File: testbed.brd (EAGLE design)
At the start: 50 x 31 mm, 22 parts, among them IC1 OPAMP-DUALMS, IC2 V_REG_MIC2920, Q1 BTS117

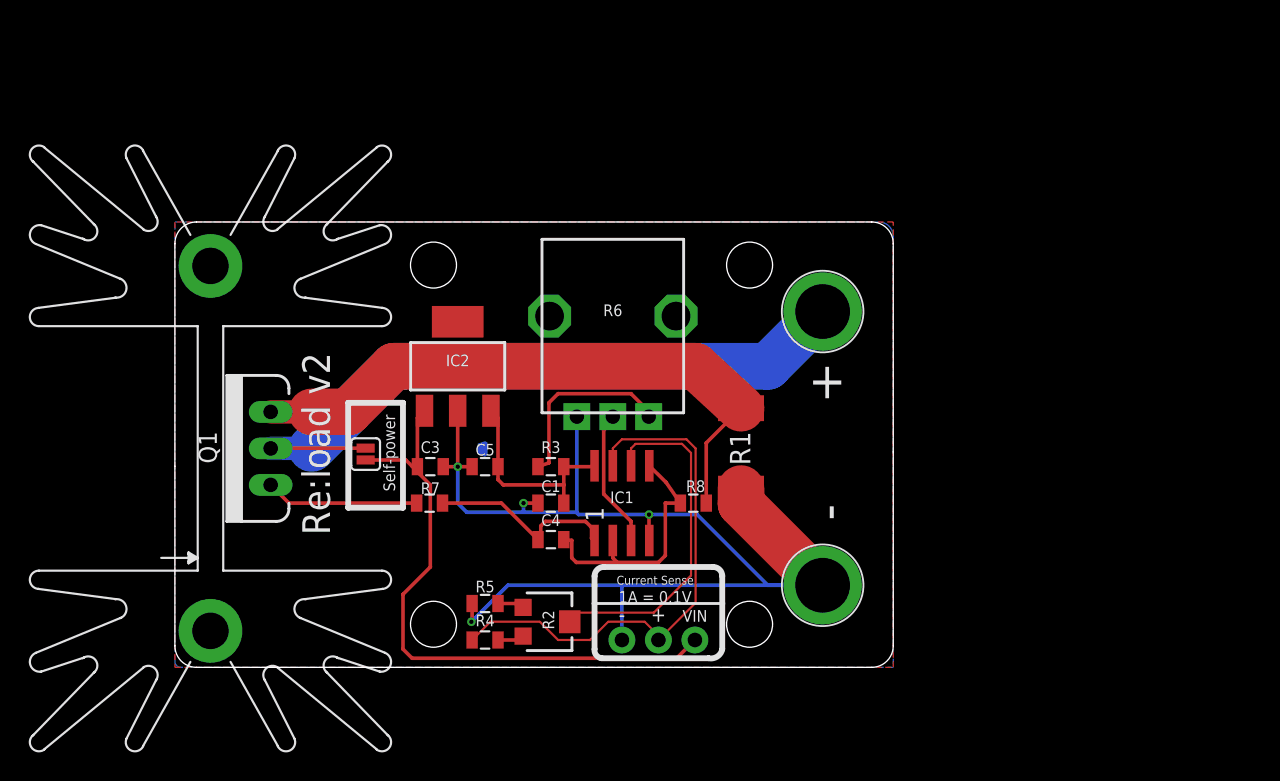
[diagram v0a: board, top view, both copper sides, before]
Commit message: Changes to SMD re:load v2; added test fixture
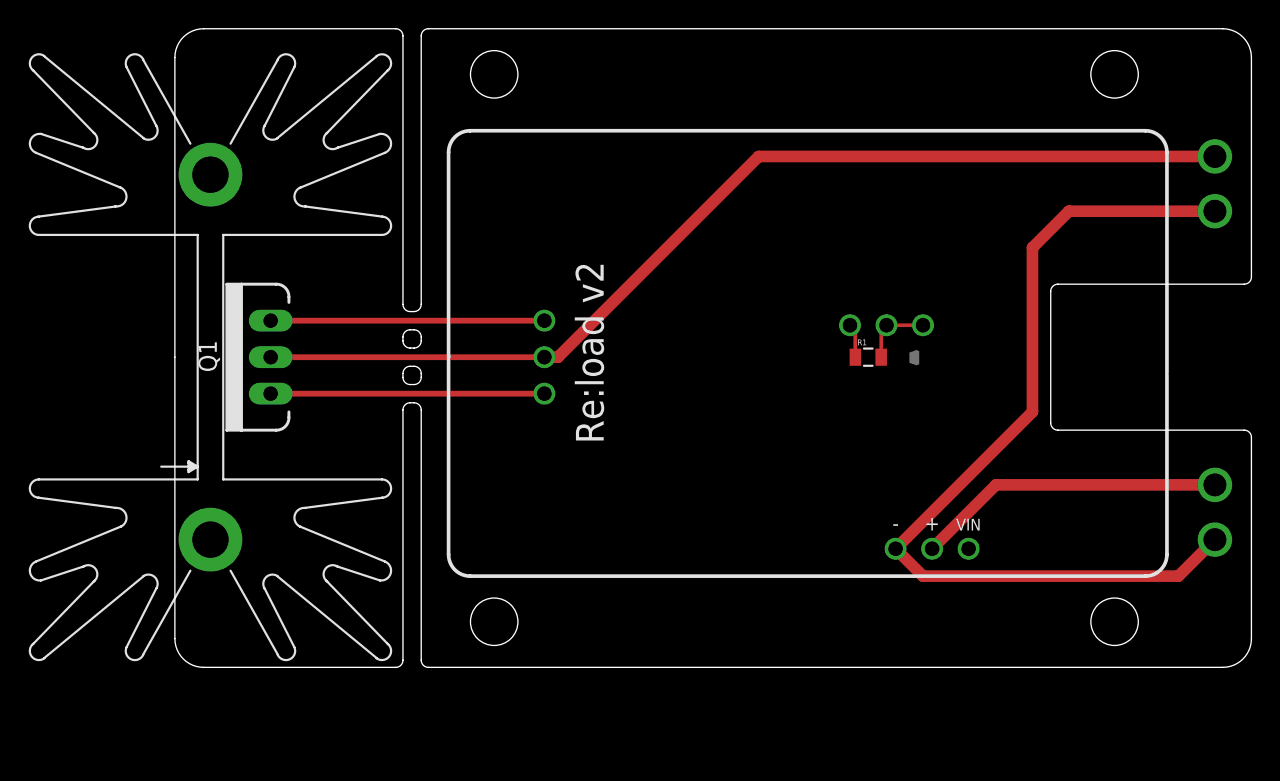
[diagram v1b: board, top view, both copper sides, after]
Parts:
- removed C1, C4: 0.1u, SparkFun-Passives:0805
- removed C3: 1u, SparkFun-Passives:0805
- removed C5: 22u, SparkFun-Passives:0805
- removed IC1: OPAMP-DUALMS, nickparts:SOP08
- removed IC2: V_REG_MIC2920, SparkFun-PowerIC:SOT223
- removed J1, J2: (no value), SparkFun-Connectors:BANANA_CONN
- removed JP1: (no value), SparkFun-Connectors:1X03_NO_SILK
- removed JP2: (no value), SparkFun-Passives:SJ_2S
- removed R2: 1k, nickparts:TRIMPOT-3MM-2
- removed R3: 162k, SparkFun-Passives:0805
- removed R4, R5, R8: 10k 1%, SparkFun-Passives:0805
- removed R6: 10k, nickparts:ALPS_POT
- removed R7: 100, SparkFun-Passives:0805
- added TEST_CURRSENSE, TEST_PGND, TEST_TGND, TEST_VIN: TEST_POINT, nickparts:TEST_POINT
- added U$1, U$14, U$15, U$4: (no value), SparkFun-Electromechanical:STAND-OFF
- added U$10, U$11, U$12, U$13, U$5, U$6, U$7, U$8, U$9: POGOPIN1.02, nickparts:POGOPIN-1.02
- R1: value 0.05 1% -> 1.27k; device SparkFun-Passives:R2512 -> SparkFun-Passives:0805
- moved U$2 30.7 mm to (50.8, 21.6)
- moved U$3 30.7 mm to (41.9, 21.6)
- moved R1 10.9 mm to (48.3, 21.6), turned to 0 degrees
- moved KK1 6.35 mm to (1.59, 21.6)
- moved Q1 6.35 mm to (6.67, 21.6)
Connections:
- removed net IREF: IC1.7, JP1.2, R4.1
- removed net N$4: IC1.3, R6.P$2
- removed net N$5: IC1.6, R2.2
- removed net N$6: R2.1, R5.1
- removed net N$7: R2.3, R4.2
- removed net SENSE: C4.2, IC1.2, IC1.5, R8.2
- removed net VCC: C1.1, C5.1, IC1.8, IC2.3, R3.2
- removed net VDD: C3.1, IC2.1, JP1.3, JP2.1
- new net N$8: R1.2, U$5.P$1, U$6.P$1
- net GND: now also TEST_PGND.P$1, TEST_TGND.P$1, U$13.P$1; no longer C1.2, C3.2, C5.2, IC1.4, IC2.2, J2.P$1, JP1.1, R1.1, R5.2, R6.P$1
- net N$1: now also Q1.1, U$8.P$1; no longer C4.1, IC1.1, R7.2
- net N$2: now also TEST_CURRSENSE.P$1, U$12.P$1; no longer R3.1, R6.P$3
- net N$3: now also U$10.P$1; no longer R1.2, R8.1
- net N$9: now also R1.1, U$7.P$1; no longer Q1.1, R7.1
- net V+: now also TEST_VIN.P$1, U$9.P$1; no longer J1.P$1, JP2.2
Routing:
- net VDD: track 43.1 -> 0.00 mm
- net IREF: track 37.2 -> 0.00 mm
- net N$5: track 24.3 -> 0.00 mm
- net GND: track 86.9 -> 62.7 mm, vias 4 -> 0
- net N$3: track 42.8 -> 19.1 mm
- net V+: track 49.4 -> 71.5 mm
- net SENSE: track 18.4 -> 0.00 mm
- net VCC: track 14.5 -> 0.00 mm
- net N$4: track 9.67 -> 0.00 mm
- net N$2: track 13.1 -> 21.5 mm
- net N$9: track 10.7 -> 2.38 mm
- net N$1: track 13.7 -> 19.1 mm
- net N$8: track 0.00 -> 4.92 mm
- net N$7: track 2.41 -> 0.00 mm
- net N$6: track 2.32 -> 0.00 mm
- removed copper zone on layer 1, net GND
- removed copper zone on layer 16, net GND
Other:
- board size 50 x 31 mm -> 74.9 x 44.5 mm
- board text removed: "1A = 0.1V"
- board text removed: "Current Sense"
- board text removed: "Self-power"
